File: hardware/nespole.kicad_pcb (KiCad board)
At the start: 2 copper layers, 41 parts, among them IC1 ATMEGA328PB-A, J1 Screw_Terminal_1x02, J2 Screw_Terminal_1x02, J3 Screw_Terminal_1x05, J4 Screw_Terminal_1x02, P1 USB_OTG, Q1 MJE13009G, Q2 MOSFET_P_CH, SW1 Rotary_Encoder_Switch, U1 MAX6675, U2 CH341T, U3 AS1108, Y1 12M

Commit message: Slightly better layout.
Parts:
- added D2: LED_RGB, LEDs:LED_RGB_PLCC-6, F.Cu at (141.4, 129.9)
- added R14: 10k, Resistors_SMD:R_0805_HandSoldering, F.Cu at (143.3, 124.8)
- added R15: 10k, Resistors_SMD:R_0805_HandSoldering, F.Cu at (145.4, 124.8)
- added R16: 10k, Resistors_SMD:R_0805_HandSoldering, F.Cu at (148.0, 126.0)
- moved J2 89.1 mm to (112.3, 150.5), turned to 270 degrees
- moved R6 88.1 mm to (111.0, 125.7), turned to 0 degrees
- moved R7 81.9 mm to (115.9, 125.7), turned to 0 degrees
- moved D1 78.5 mm to (111.1, 145.8), turned to 90 degrees
- moved C9 77.3 mm to (112.2, 102.6), turned to 180 degrees
- moved Q1 77.3 mm to (112.2, 140.5), turned to 90 degrees
- moved R2 74.4 mm to (108.8, 140.4), turned to 90 degrees
- moved R1 72.1 mm to (108.8, 133.7), turned to 270 degrees
- moved SW1 71.0 mm to (119.2, 114.1), turned to 90 degrees
- moved J1 65.2 mm to (186.2, 120.7), turned to 90 degrees
- moved R9 57.1 mm to (132.2, 118.9), turned to 180 degrees
- moved R11 55.4 mm to (132.2, 116.6), turned to 0 degrees
- moved P1 55.4 mm to (175.6, 106.3), turned to 270 degrees
- moved C10 53.9 mm to (132.2, 114.1), turned to 0 degrees
- moved R4 52.7 mm to (186.7, 129.8), turned to 0 degrees
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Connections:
- C9 pad 2: Net-(C9-Pad2) -> SW_BUTTON
- IC1 pad 10: TEMP_CS -> LED_G
- IC1 pad 13: Net-(IC1-Pad13) -> LED_B
- IC1 pad 19: Net-(IC1-Pad19) -> TEMP_CS
- IC1 pad 22: Net-(IC1-Pad22) -> LED_CS
- IC1 pad 9: LED_CS -> LED_R
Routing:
- net SW_DIR: track 113.0 -> 27.3 mm, vias 2 -> 3
- net SW_INT: track 124.7 -> 45.8 mm, vias 0 -> 2
- net SW_BUTTON: track 122.3 -> 82.9 mm, vias 6 -> 2
- net RESET: track 32.7 -> 65.9 mm, vias 2 -> 4
- net GND: track 86.5 -> 117.6 mm, vias 16 -> 15
- net Net-(AFF1-Pad7): track 58.0 -> 29.5 mm
- net +5V: track 276.7 -> 252.2 mm, vias 8 -> 9
- net Net-(AFF1-Pad6): track 29.3 -> 53.3 mm
- net MC_CS: track 32.9 -> 11.4 mm, vias 3 -> 1
- net Net-(AFF1-Pad11): track 32.4 -> 52.9 mm
- net Net-(R12-Pad2): track 5.44 -> 23.6 mm, vias 0 -> 2
- net SCK: track 81.0 -> 63.2 mm, vias 6 -> 4
- net Net-(C9-Pad1): track 28.4 -> 42.4 mm
- net Net-(AFF1-Pad2): track 54.6 -> 40.6 mm
- net LED_B: track 0.00 -> 11.6 mm, vias 0 -> 2
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
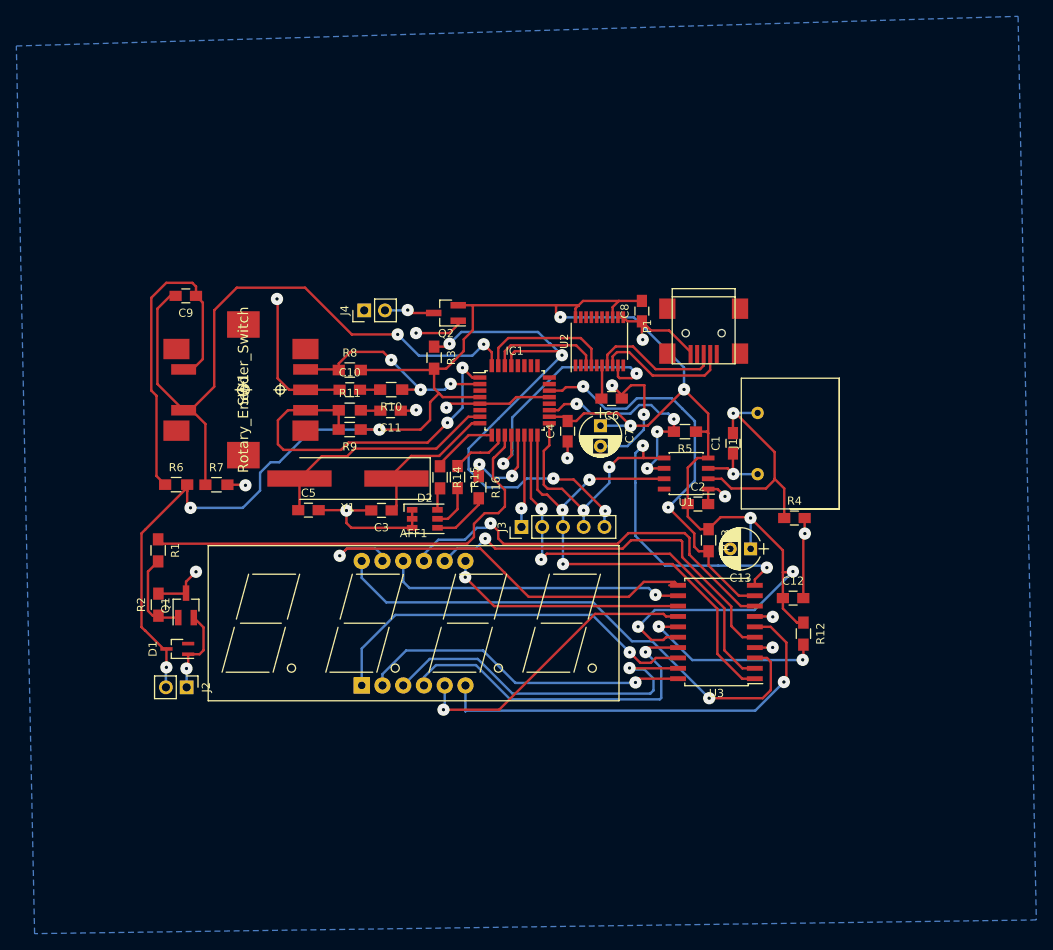
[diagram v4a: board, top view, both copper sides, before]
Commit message: Cutting groundplane to size; adding edge cuts.
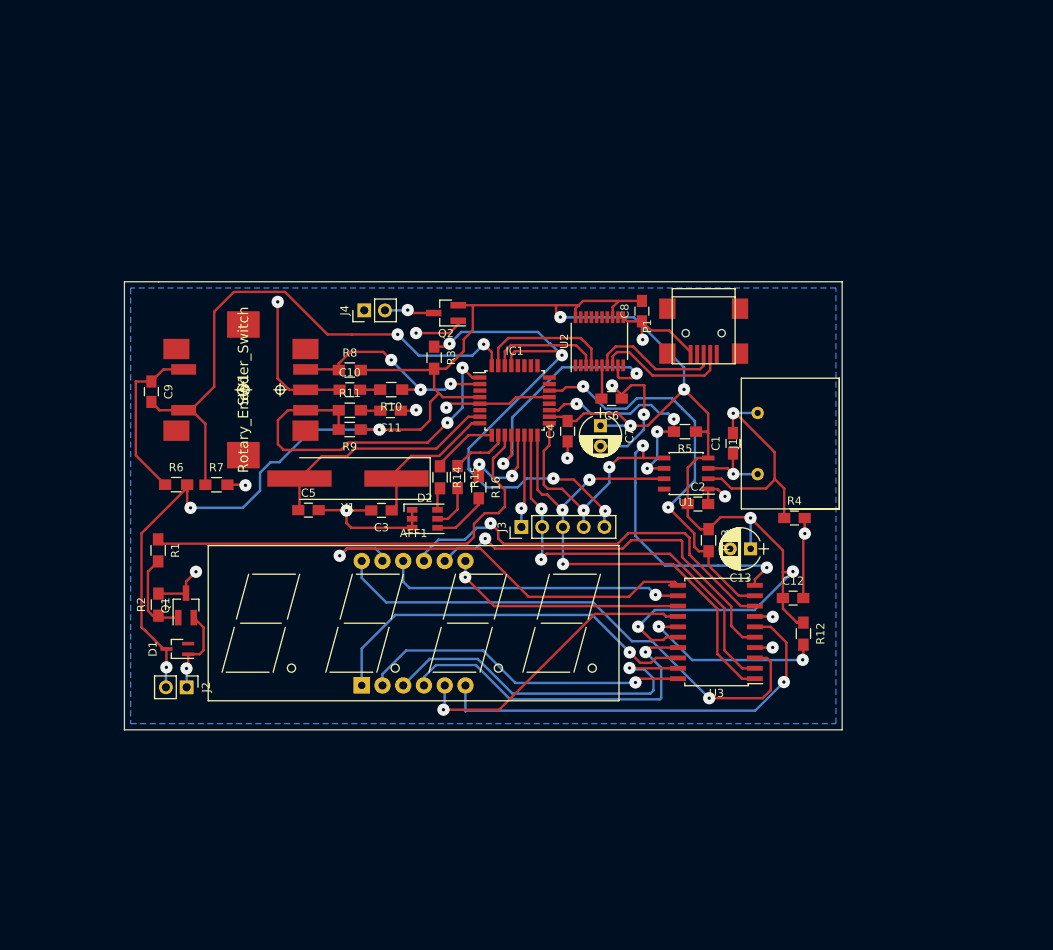
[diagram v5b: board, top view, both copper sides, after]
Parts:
- moved C9 12.5 mm to (108.0, 114.3), turned to 270 degrees
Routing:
- net Net-(C9-Pad1): track 42.4 -> 22.0 mm
- net SW_BUTTON: track 82.9 -> 70.1 mm
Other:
- board outline added: 87.9 x 54.9 mm
